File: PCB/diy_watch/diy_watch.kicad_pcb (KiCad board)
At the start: 2 copper layers, 37 x 37 mm, 19 parts, among them P1 USB_C_Plug_USB2.0, SW1 SW_Push, U1 W25Q32JVSS, U2 DS3231MZ, U3 RP2040, Y1 12MHz_crystal

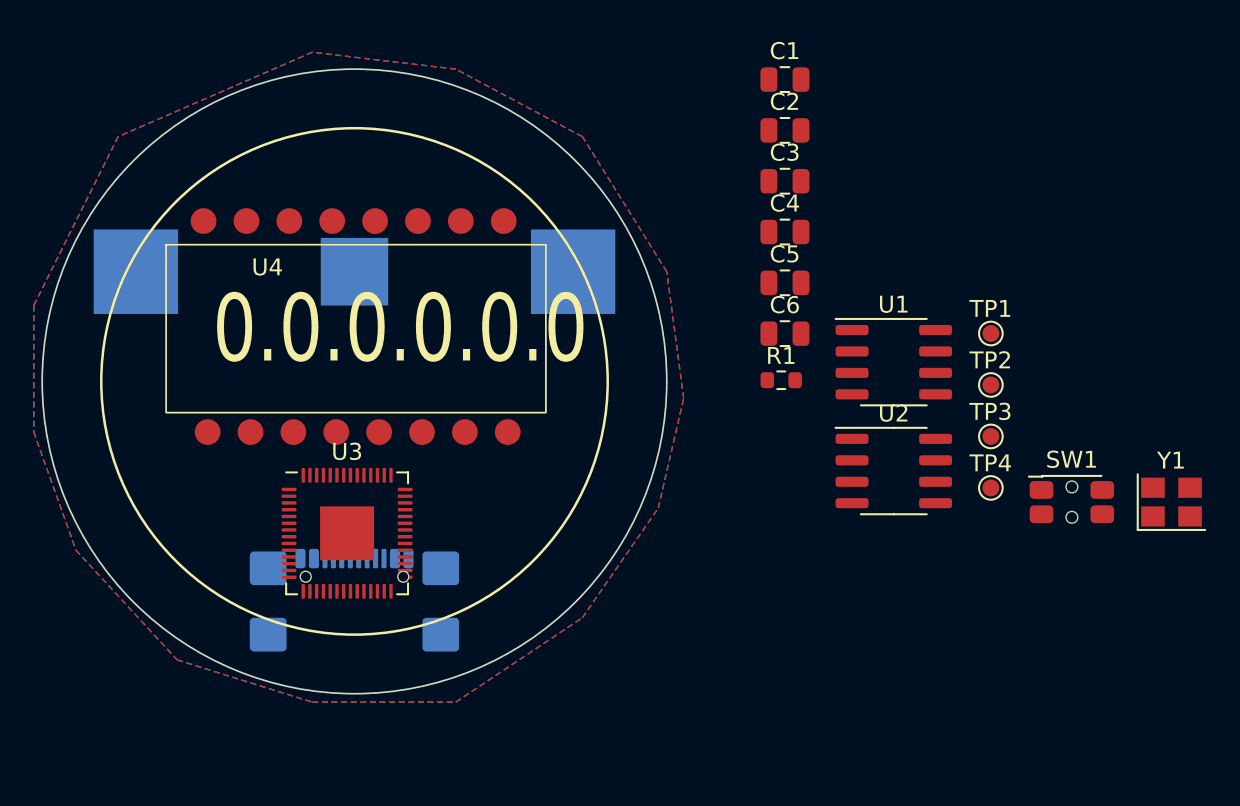
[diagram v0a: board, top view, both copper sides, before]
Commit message: Updating watch PCB
Added COM resistor pullup/downs
Added switch
Added LEDs
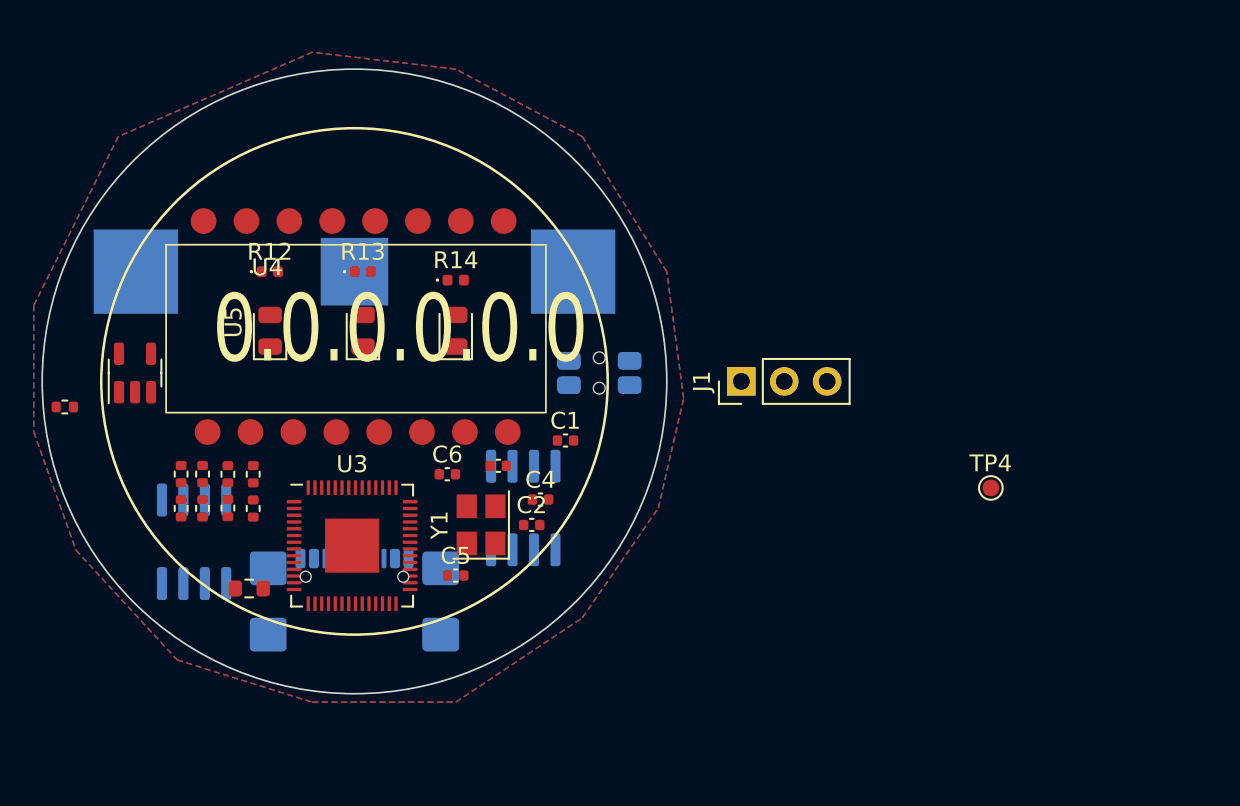
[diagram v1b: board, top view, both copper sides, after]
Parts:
- removed TP1, TP2, TP3: TestPoint, TestPoint:TestPoint_Pad_D1.0mm
- added D1: LED, LED_SMD:LED_0805_2012Metric, F.Cu at (145.0, 97.0)
- added D2: LED, LED_SMD:LED_0805_2012Metric, F.Cu at (150.5, 97.0)
- added D3: LED, LED_SMD:LED_0805_2012Metric, F.Cu at (156.0, 97.0)
- added J1: Debug Port, Connector_PinHeader_2.54mm:PinHeader_1x03_P2.54mm_Vertical, F.Cu at (172.9, 100.0)
- added R10: 5K, Resistor_SMD:R_0402_1005Metric, F.Cu at (142.5, 107.5)
- added R12: 300, LED_SMD:LED_0402_1005Metric, F.Cu at (145.0, 93.5)
- added R13: 300, LED_SMD:LED_0402_1005Metric, F.Cu at (150.5, 93.5)
- added R14: 300, LED_SMD:LED_0402_1005Metric, F.Cu at (156.0, 94.0)
- added R2: R, Resistor_SMD:R_0402_1005Metric, F.Cu at (132.8, 101.5)
- added R3: 5K, Resistor_SMD:R_0402_1005Metric, F.Cu at (139.7, 105.5)
- added R4: 5K, Resistor_SMD:R_0402_1005Metric, F.Cu at (139.7, 107.5)
- added R5: 5K, Resistor_SMD:R_0402_1005Metric, F.Cu at (141.0, 105.5)
- added R6: 5K, Resistor_SMD:R_0402_1005Metric, F.Cu at (141.0, 107.5)
- added R7: 5K, Resistor_SMD:R_0402_1005Metric, F.Cu at (144.0, 105.5)
- added R8: 5K, Resistor_SMD:R_0402_1005Metric, F.Cu at (144.0, 107.5)
- added R9: 5K, Resistor_SMD:R_0402_1005Metric, F.Cu at (142.5, 105.5)
- added U5: LTC4054ES5-4.2, Package_TO_SOT_SMD:TSOT-23-5, F.Cu at (137.0, 99.5)
- C1, C2, C3, C4, C5, C6: footprint Capacitor_SMD:C_0805_2012Metric -> Capacitor_SMD:C_0402_1005Metric
- SW1, U1, U2: moved to B.Cu
- moved U1 42.8 mm to (140.5, 109.5), turned to 90 degrees
- moved Y1 40.9 mm to (157.5, 108.5), turned to 90 degrees
- moved R1 33.8 mm to (143.8, 112.3), turned to 180 degrees
- moved SW1 29.0 mm to (164.5, 99.5), turned to 180 degrees
- moved C2 27.8 mm to (160.5, 108.5)
- moved C5 26.1 mm to (156.0, 111.5)
- moved C1 25.0 mm to (162.5, 103.5)
- moved C3 23.9 mm to (158.5, 105.0)
- moved U2 22.1 mm to (160.0, 107.5), turned to -90 degrees
- moved C6 21.7 mm to (155.5, 105.5)
- moved C4 21.5 mm to (161.0, 107.0)
- moved U3 0.79 mm to (149.9, 109.7)
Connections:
- net Net-(P1-VBUS-PadA4) renamed +5V
- BT1 pad 1: unconnected-(BT1-+-Pad1) -> +BATT
- BT1 pad 2: unconnected-(BT1---Pad2) -> GND
- P1 pad A1: Net-(P1-GND-PadA1) -> GND
- P1 pad A12: Net-(P1-GND-PadA1) -> GND
- P1 pad A6: unconnected-(P1-D+-PadA6) -> /usb_D+
- P1 pad A7: unconnected-(P1-D--PadA7) -> /usb_D-
- P1 pad B1: Net-(P1-GND-PadA1) -> GND
- P1 pad B12: Net-(P1-GND-PadA1) -> GND
- U2 pad 2: unconnected-(U2-VCC-Pad2) -> +3.3V
- U2 pad 3: unconnected-(U2-~{INT}/SQW-Pad3) -> /RTC_INT
- U2 pad 4: unconnected-(U2-~{RST}-Pad4) -> +3V3
- U2 pad 5: unconnected-(U2-GND-Pad5) -> GND
- U2 pad 6: unconnected-(U2-VBAT-Pad6) -> +BATT
- U2 pad 7: unconnected-(U2-SDA-Pad7) -> /RTC_SDA
- U2 pad 8: unconnected-(U2-SCL-Pad8) -> /RTC_SCL
- U3 pad 11: unconnected-(U3-GPIO8-Pad11) -> /E
- U3 pad 12: unconnected-(U3-GPIO9-Pad12) -> /F
- U3 pad 13: unconnected-(U3-GPIO10-Pad13) -> /G
- U3 pad 14: unconnected-(U3-GPIO11-Pad14) -> /H
- U3 pad 15: unconnected-(U3-GPIO12-Pad15) -> /I
- U3 pad 16: unconnected-(U3-GPIO13-Pad16) -> /J
- U3 pad 17: unconnected-(U3-GPIO14-Pad17) -> /K
- U3 pad 18: unconnected-(U3-GPIO15-Pad18) -> /L
- U3 pad 2: unconnected-(U3-GPIO0-Pad2) -> /COM1
- U3 pad 27: unconnected-(U3-GPIO16-Pad27) -> /RTC_SDA
- U3 pad 28: unconnected-(U3-GPIO17-Pad28) -> /RTC_SCL
- U3 pad 29: unconnected-(U3-GPIO18-Pad29) -> /RTC_INT
- U3 pad 3: unconnected-(U3-GPIO1-Pad3) -> /COM2
- U3 pad 30: unconnected-(U3-GPIO19-Pad30) -> /light_sw
- U3 pad 4: unconnected-(U3-GPIO2-Pad4) -> /COM3
- U3 pad 5: unconnected-(U3-GPIO3-Pad5) -> /COM4
- U3 pad 6: unconnected-(U3-GPIO4-Pad6) -> /A
- U3 pad 7: unconnected-(U3-GPIO5-Pad7) -> /B
- U3 pad 8: unconnected-(U3-GPIO6-Pad8) -> /C
- U3 pad 9: unconnected-(U3-GPIO7-Pad9) -> /D
- U4 pad 1: unconnected-(U4-COM1-Pad1) -> /COM1
- U4 pad 10: unconnected-(U4-F-Pad10) -> /F
- U4 pad 11: unconnected-(U4-G-Pad11) -> /G
- U4 pad 12: unconnected-(U4-H-Pad12) -> /H
- U4 pad 13: unconnected-(U4-I-Pad13) -> /I
- U4 pad 14: unconnected-(U4-J-Pad14) -> /J
- U4 pad 15: unconnected-(U4-K-Pad15) -> /K
- U4 pad 16: unconnected-(U4-L-Pad16) -> /L
- U4 pad 2: unconnected-(U4-COM2-Pad2) -> /COM2
- U4 pad 3: unconnected-(U4-COM3-Pad3) -> /COM3
- U4 pad 4: unconnected-(U4-COM4-Pad4) -> /COM4
- U4 pad 5: unconnected-(U4-A-Pad5) -> /A
- U4 pad 6: unconnected-(U4-B-Pad6) -> /B
- U4 pad 7: unconnected-(U4-C-Pad7) -> /C
- U4 pad 8: unconnected-(U4-D-Pad8) -> /D
- U4 pad 9: unconnected-(U4-E-Pad9) -> /E

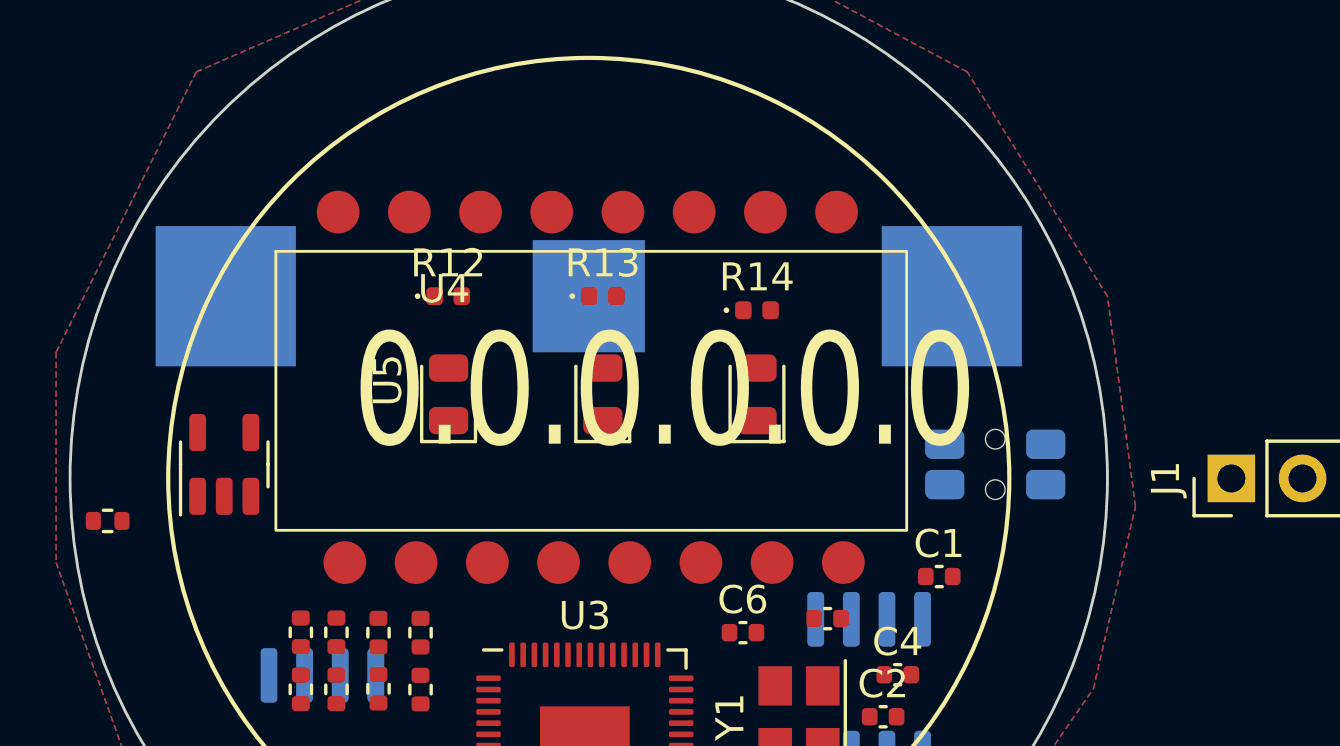
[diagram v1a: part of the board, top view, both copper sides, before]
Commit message: Updated swich layout and symbol
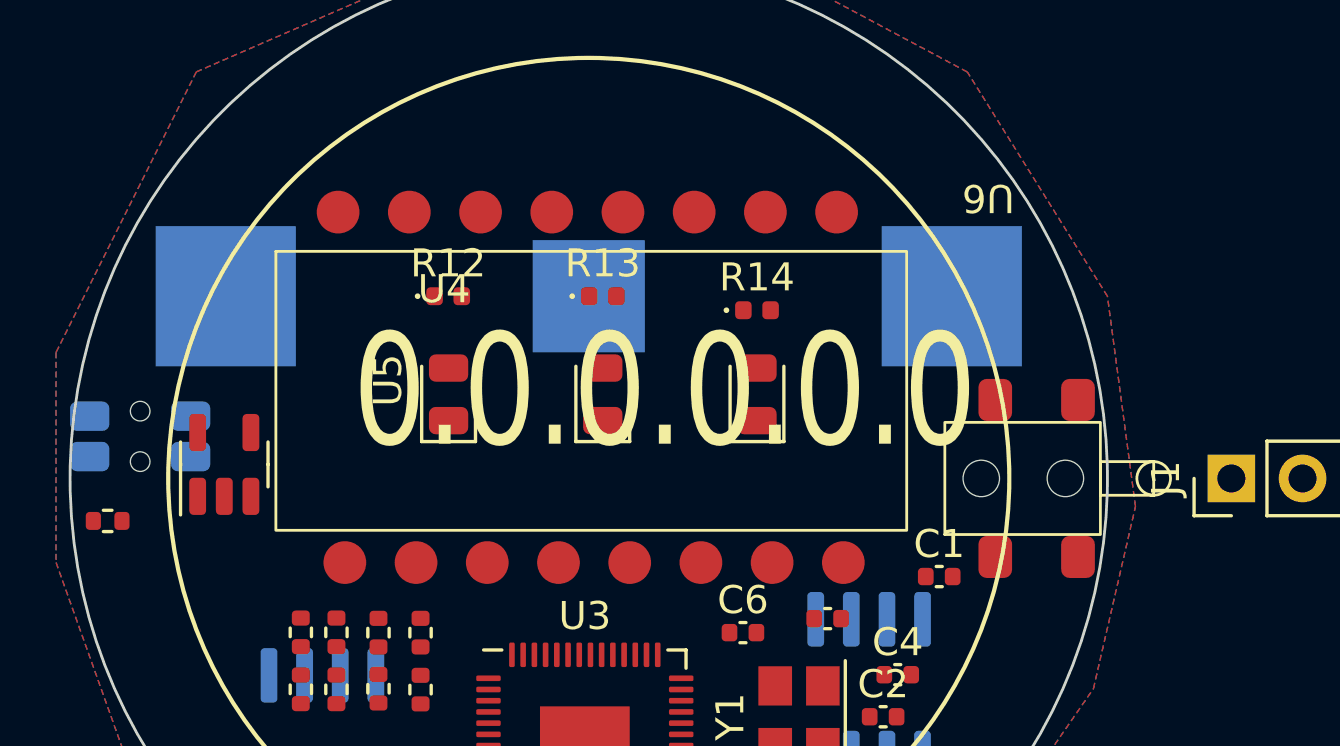
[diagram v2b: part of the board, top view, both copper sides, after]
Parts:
- added U6: ~, DIY_Watch_lib:Diptronics FTE-3, F.Cu at (164.5, 100.0)
- moved SW1 30.5 mm to (134.0, 98.5)
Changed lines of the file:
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@@
   (net 59 "/RTC_SCL")
   (net 60 "/light_sw")
+  (net 61 "unconnected-(U6-Pad2)")
+  (net 62 "unconnected-(U6-Pad4)")
   (footprint "Capacitor_SMD:C_0402_1005Metric" (layer "F.Cu")
     (at 156 111.5)
@@
     )
   )
+  (footprint "DIY_Watch_lib:Diptronics FTE-3" (layer "F.Cu")
+    (at 164.5 100 180)
+    (property "Sheetfile" "diy_watch.kicad_sch")
+    (property "Sheetname" "")
+    (attr smd)
+    (fp_text reference "U6" (at 0.25 10 180 unlocked) (layer "F.SilkS")
+        (effects (font (size 1 1) (thickness 0.1)))
+    )
+    (fp_text value "~" (at 0.25 13.5 180 unlocked) (layer "F.Fab")
+        (effects (font (size 1 1) (thickness 0.15)))
+    )
+    (fp_text user "${REFERENCE}" (at -0.5 11.5 180 unlocked) (layer "F.Fab")
+        (effects (font (size 1 1) (thickness 0.15)))
+    )
+    (fp_rect (start -5.65 -0.6) (end -3.75 0.6)
+      (stroke (width 0.1) (type default)) (fill none) (layer "F.SilkS"))
+    (fp_rect (start 1.8 -2) (end -3.75 2)
+      (stroke (width 0.1) (type default)) (fill none) (layer "F.SilkS"))
+    (fp_circle (center -5.65 0) (end -5.65 -0.6)
+      (stroke (width 0.1) (type default)) (fill none) (layer "F.SilkS"))
+    (pad "" np_thru_hole circle (at -2.5 0 270) (size 0.9 0.9) (drill 1.3) (layers "F&B.Cu" "*.Mask"))
+    (pad "" np_thru_hole circle (at 0.5 0 270) (size 0.9 0.9) (drill 1.3) (layers "F&B.Cu" "*.Mask"))
+    (pad "1" smd roundrect (at -2.95 -2.8 270) (size 1.5 1.2) (layers "F.Cu" "F.Paste" "F.Mask") (roundrect_rratio 0.25)
+      (net 60 "/light_sw") (pintype "passive") (thermal_bridge_angle 45))
+    (pad "2" smd roundrect (at 0 -2.8 270) (size 1.5 1.2) (layers "F.Cu" "F.Paste" "F.Mask") (roundrect_rratio 0.25)
+      (net 61 "unconnected-(U6-Pad2)") (pintype "passive+no_connect") (thermal_bridge_angle 45))
+    (pad "3" smd roundrect (at -2.95 2.8 270) (size 1.5 1.2) (layers "F.Cu" "F.Paste" "F.Mask") (roundrect_rratio 0.25)
+      (net 2 "GND") (pintype "passive") (thermal_bridge_angle 45))
+    (pad "4" smd roundrect (at 0 2.8 270) (size 1.5 1.2) (layers "F.Cu" "F.Paste" "F.Mask") (roundrect_rratio 0.25)
+      (net 62 "unconnected-(U6-Pad4)") (pintype "passive+no_connect") (thermal_bridge_angle 45))
+  )
   (footprint "Capacitor_SMD:C_0402_1005Metric" (layer "F.Cu")
     (at 155.5 105.5)
@@
   )
   (footprint "Button_Switch_SMD:SW_SPST_EVQP7C" (layer "B.Cu")
-    (at 164.5 99.5 180)
+    (at 134 98.5 180)
     (descr "Light Touch Switch, 2.2 N, https://www3.panasonic.biz/ac/e_download/control/switch/light-touch/catalog/sw_lt_eng_3529s_side.pdf?f_cd=402906")
     (tags "tactile switch")

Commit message: Routed most of the PCB, big staggetti
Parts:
- removed P1: USB_C_Plug_USB2.0, Connector_USB:USB_C_Receptacle_GCT_USB4110
- added TP1: TP_SWCLK, TestPoint:TestPoint_Pad_D1.5mm, B.Cu at (146.3, 116.6)
- added TP2: TP_GND, TestPoint:TestPoint_Pad_D1.5mm, B.Cu at (151.9, 116.6)
- added TP3: TP_SWD, TestPoint:TestPoint_Pad_D1.5mm, B.Cu at (149.1, 116.6)
- added TP5: TP_3V3, TestPoint:TestPoint_Pad_D1.5mm, B.Cu at (143.8, 115.6)
- added U7: XC6210B332MR, Package_TO_SOT_SMD:SOT-23-5, F.Cu at (160.5, 99.1)
- J1: value Debug Port -> USB_B_Micro; footprint Connector_PinHeader_2.54mm:PinHeader_1x03_P2.54mm_Vertical -> Connector_USB:USB_Micro-B_GCT_USB3076-30-A; moved to B.Cu
- TP4, U6: moved to B.Cu
- moved J1 37.7 mm to (135.2, 101.4)
- moved TP4 34.7 mm to (154.4, 116.3), turned to 180 degrees
- moved C1 17.7 mm to (145.0, 106.4), turned to 90 degrees
- moved R2 11.9 mm to (140.7, 110.5), turned to 180 degrees
- moved C4 11.5 mm to (149.9, 104.4), turned to 180 degrees
- moved SW1 10.8 mm to (137.3, 108.8), turned to 90 degrees
- moved C5 8.12 mm to (151.6, 104.6)
- moved C3 7.41 mm to (156.6, 112.1)
- moved C2 4.54 mm to (156.5, 106.4), turned to 180 degrees
- moved R7 3.79 mm to (140.2, 105.4)
- moved R8 3.79 mm to (140.2, 107.4)
- moved R10 3.56 mm to (138.9, 107.4)
- moved R9 3.56 mm to (138.9, 105.4)
- moved R3 3.02 mm to (142.7, 105.4)
- moved R4 3.02 mm to (142.7, 107.4)
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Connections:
- J1 pad 1: Net-(J1-Pin_1) -> +5V
- J1 pad 2: GND -> /usb_D-
- J1 pad 3: Net-(J1-Pin_3) -> /usb_D+
- R3 pad 1: +3V3 -> +3.3V
- R5 pad 1: +3V3 -> +3.3V
- R7 pad 1: +3V3 -> +3.3V
- R9 pad 1: +3V3 -> +3.3V
- U2 pad 4: +3V3 -> +3.3V
- U3 pad 24: Net-(J1-Pin_1) -> Net-(U3-SWCLK)
- U3 pad 25: Net-(J1-Pin_3) -> Net-(U3-SWD)
- U3 pad 31: unconnected-(U3-GPIO20-Pad31) -> /light_en
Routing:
- net +BATT: track 0.00 -> 66.2 mm, vias 0 -> 3
- net +3.3V: track 0.00 -> 50.4 mm, vias 0 -> 4
- net /L: track 0.00 -> 42.4 mm, vias 0 -> 2
- net /K: track 0.00 -> 39.1 mm, vias 0 -> 2
- net /J: track 0.00 -> 35.0 mm, vias 0 -> 2
- net /I: track 0.00 -> 31.9 mm, vias 0 -> 2
- net /F: track 0.00 -> 31.5 mm, vias 0 -> 2
- net /E: track 0.00 -> 31.3 mm, vias 0 -> 2
- net /light_sw: track 0.00 -> 30.2 mm, vias 0 -> 3
- net /usb_D-: track 0.00 -> 28.9 mm, vias 0 -> 4
- net /usb_D+: track 0.00 -> 26.5 mm, vias 0 -> 3
- net /H: track 0.00 -> 26.4 mm, vias 0 -> 2
- net /G: track 0.00 -> 26.3 mm, vias 0 -> 2
- net /COM4: track 0.00 -> 26.0 mm
- net +5V: track 0.00 -> 25.7 mm
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- added copper zone on B.Cu, net GND
- added copper zone on F.Cu, net GND
- removed copper zone on B.Cu, net (none)
- removed copper zone on F.Cu, net (none)
